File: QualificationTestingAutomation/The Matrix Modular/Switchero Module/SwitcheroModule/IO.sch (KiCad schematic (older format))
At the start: 8 parts, among them J1 Conn_02x32_Counter_Clockwise_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, J2 OBD Connector, J3 OBD Connector, J6 Conn_02x32_Counter_Clockwise_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

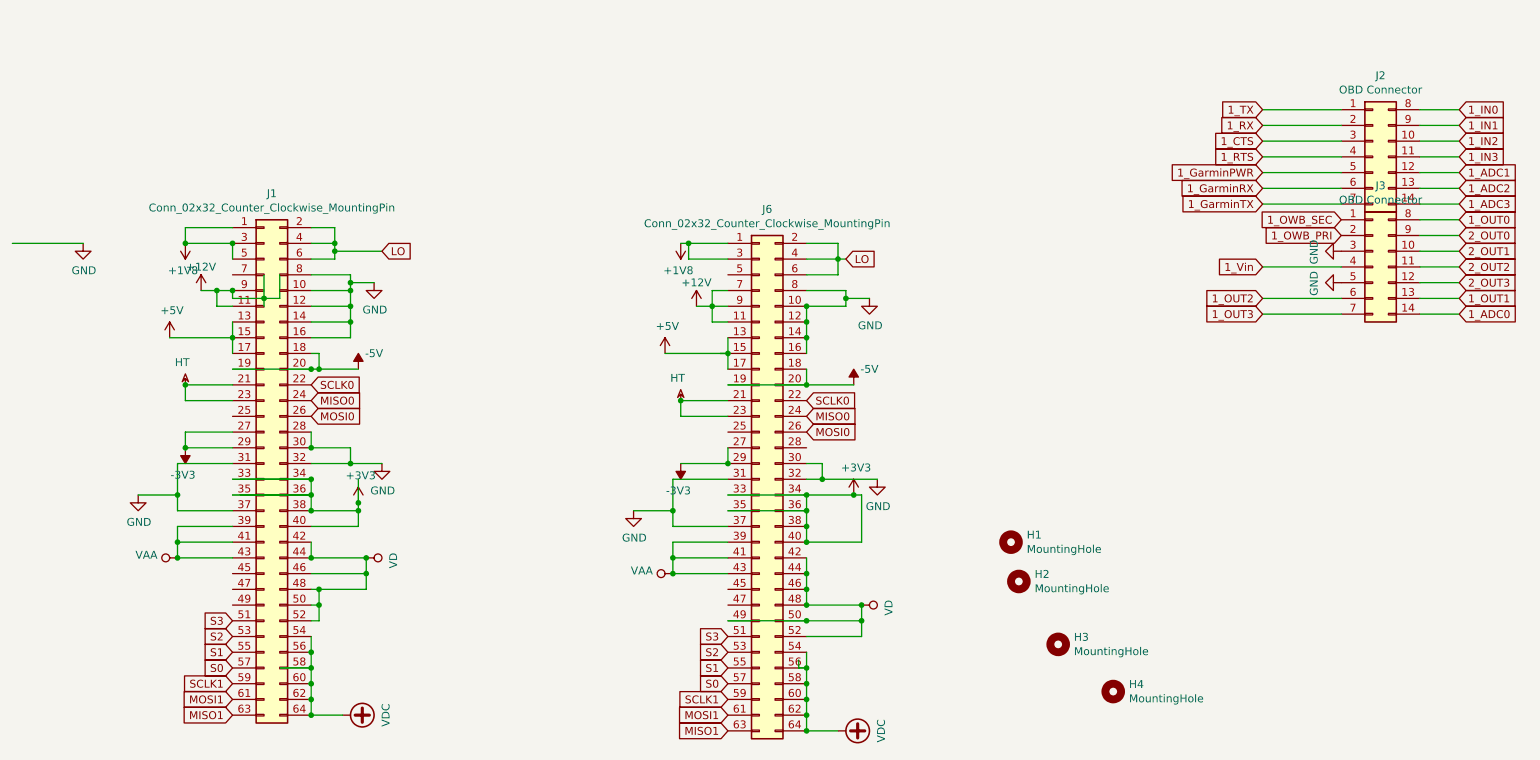
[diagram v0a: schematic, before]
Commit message: Cleaned up the libraries Cleaned up the tracks Adjusted footprints to the manufacturers minimum size.
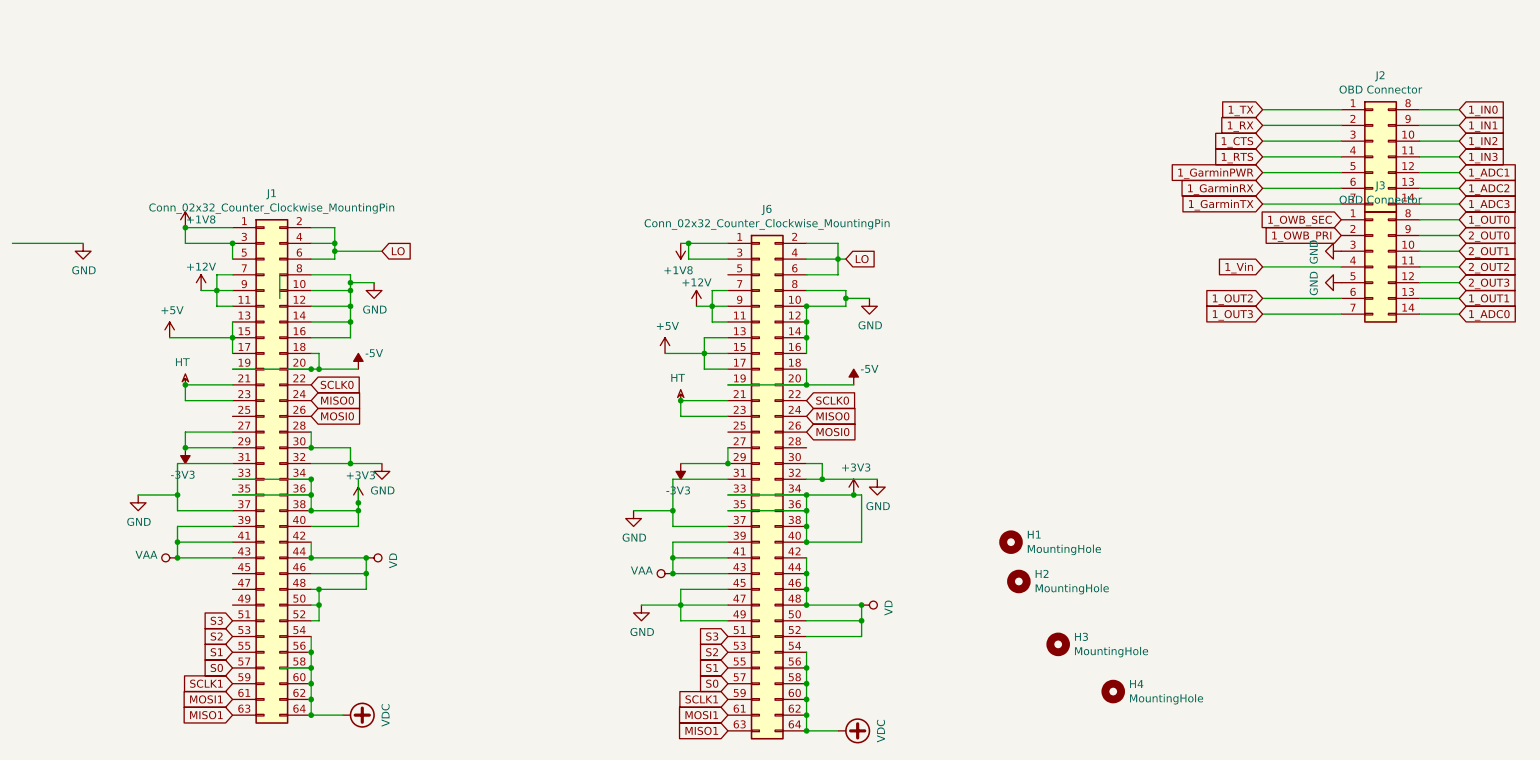
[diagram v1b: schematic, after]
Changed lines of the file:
@@
 L power:+1V8 #PWR?
 U 1 1 5DFE913D
-P 2450 2200
+P 2450 2100
 AR Path="/5D94288A/5DFE913D" Ref="#PWR?"  Part="1"
 AR Path="/5D968A33/5DFE913D" Ref="#PWR?"  Part="1"
 AR Path="/5C90F517/5DFE913D" Ref="#PWR0181"  Part="1"
-F 0 "#PWR0181" H 2450 2050 50  0001 C CNN
-F 1 "+1V8" H 2465 2373 50  0000 C CNN
-F 2 "" H 2450 2200 50  0001 C CNN
-F 3 "" H 2450 2200 50  0001 C CNN
-	1    2450 2200
-	-1   0    0    1
+F 0 "#PWR0181" H 2450 1950 50  0001 C CNN
+F 1 "+1V8" H 2550 2150 50  0000 C CNN
+F 2 "" H 2450 2100 50  0001 C CNN
+F 3 "" H 2450 2100 50  0001 C CNN
+	1    2450 2100
+	1    0    0    -1
 $EndComp
 $Comp
@@
 Wire Wire Line
 	2450 2100 2750 2100
-Connection ~ 2450 2200
 $Comp
 L power:GND #PWR0183
@@
 Wire Wire Line
 	3050 2400 3050 2550
-Wire Wire Line
-	3050 2550 2950 2550
 Wire Wire Line
 	3250 2300 3400 2300
@@
 	1    0    0    -1
 $EndComp
-Wire Wire Line
-	5900 3000 5900 2900
 Text GLabel 5900 5000 0    50   Input ~ 0
 S0
@@
 Text GLabel 6400 3300 2    50   Input ~ 0
 MISO0
-Connection ~ 5900 2900
 Connection ~ 5600 3200
-Wire Wire Line
-	5900 2800 5900 2900
 Text GLabel 5900 4700 0    50   Input ~ 0
 S3
@@
 	3250 5200 3450 5200
 Connection ~ 3250 4900
-Wire Wire Line
-	3250 4800 3250 4700
-Connection ~ 3250 4800
 Connection ~ 3250 3800
 Wire Wire Line
@@
 Wire Wire Line
 	5600 3600 5900 3600
-Wire Wire Line
-	6350 4850 6350 4900
 Wire Wire Line
 	5900 3600 5900 3500
@@
 	5650 2200 5900 2200
 Wire Wire Line
-	3250 4800 3250 4900
-Wire Wire Line
 	6400 3600 6500 3600
 Wire Wire Line
@@
 Wire Wire Line
 	3500 3600 3700 3600
-Wire Wire Line
-	6400 4900 6350 4900
 Wire Wire Line
 	3050 4900 3250 4900
@@
 Wire Wire Line
 	5900 3800 6400 3800
-Wire Wire Line
-	2800 3800 3250 3800
-Wire Wire Line
-	2750 3800 3250 3800
 Wire Wire Line
 	5900 3900 6400 3900
@@
 Wire Wire Line
 	6400 4600 6750 4600
-Wire Wire Line
-	5900 4600 6400 4600
 Connection ~ 6400 4100
 Wire Wire Line
@@
 Connection ~ 6400 3100
 Wire Wire Line
-	5850 2900 5900 2900
-Wire Wire Line
-	5500 2900 5900 2900
-Wire Wire Line
 	3250 3400 3250 3500
 Connection ~ 3550 3850
@@
 	3300 4400 3600 4400
 Wire Wire Line
-	2950 2550 2950 2600
-Wire Wire Line
-	2950 2400 2950 2550
-Connection ~ 2950 2550
-Wire Wire Line
-	2750 2550 2750 2500
-Wire Wire Line
-	2750 2550 2950 2550
-Connection ~ 2750 2500
+	2750 3700 3250 3700
+Wire Wire Line
+	3550 3000 3300 3000
+Wire Wire Line
+	3300 4500 3250 4500
+Wire Wire Line
+	3250 4600 3300 4600
+Wire Wire Line
+	3300 4600 3300 4500
+Connection ~ 3300 4500
+Wire Wire Line
+	3250 4100 3250 4200
+Wire Wire Line
+	3500 2500 3500 2600
+Wire Wire Line
+	3500 2600 3250 2600
+Connection ~ 3500 2500
+Wire Wire Line
+	3250 2700 3500 2700
+Wire Wire Line
+	3500 2700 3500 2600
+Connection ~ 3500 2600
+Wire Wire Line
+	3250 2800 3500 2800
+Wire Wire Line
+	3500 2800 3500 2700
+Connection ~ 3500 2700
+Wire Wire Line
+	3300 2900 3300 3000
+Connection ~ 3300 3000
+Wire Wire Line
+	6400 4200 6400 4300
+Connection ~ 6400 4500
+Connection ~ 6400 4300
+Wire Wire Line
+	6400 4300 6400 4400
+Connection ~ 6400 4400
+Wire Wire Line
+	6400 4400 6400 4500
+Wire Wire Line
+	6400 2600 6400 2700
+Connection ~ 6400 2600
+Connection ~ 6400 2700
+Wire Wire Line
+	6400 2700 6400 2800
+Connection ~ 6400 2800
+Wire Wire Line
+	6400 2800 6400 2900
+Wire Wire Line
+	6400 3100 6400 3000
+Wire Wire Line
+	2750 2800 2350 2800
+Wire Wire Line
+	2750 3800 3250 3800
 Connection ~ 3250 5200
 Wire Wire Line
@@
 Connection ~ 3250 5100
 Wire Wire Line
+	3250 4900 3250 5000
+Wire Wire Line
 	3250 5000 3250 5100
-Wire Wire Line
-	3250 4900 3250 5000
 Connection ~ 3250 5000
+Wire Wire Line
+	3250 4800 3250 4900
+Wire Wire Line
+	3250 4800 3250 4700
+Connection ~ 3250 4800
+Connection ~ 3250 4200
 Connection ~ 3250 3900
-Wire Wire Line
-	2750 3700 3250 3700
-Wire Wire Line
-	2800 3700 3250 3700
 Connection ~ 3250 3700
 Connection ~ 3250 3500
 Connection ~ 2750 2200
 Wire Wire Line
+	3300 3000 3250 3000
+Wire Wire Line
 	2750 3000 3250 3000
-Wire Wire Line
-	3550 3000 3300 3000
 Connection ~ 3250 3000
 $Comp
@@
 	1    0    0    -1
 $EndComp
-Wire Wire Line
-	3300 4500 3250 4500
-Wire Wire Line
-	3250 4600 3300 4600
-Wire Wire Line
-	3300 4600 3300 4500
-Connection ~ 3300 4500
-Wire Wire Line
-	3250 4100 3250 4200
-Connection ~ 3250 4200
-Wire Wire Line
-	3500 2500 3500 2600
-Wire Wire Line
-	3500 2600 3250 2600
-Connection ~ 3500 2500
-Wire Wire Line
-	3250 2700 3500 2700
-Wire Wire Line
-	3500 2700 3500 2600
-Connection ~ 3500 2600
-Wire Wire Line
-	3250 2800 3500 2800
-Wire Wire Line
-	3500 2800 3500 2700
-Connection ~ 3500 2700
-Wire Wire Line
-	3300 2900 3300 3000
-Connection ~ 3300 3000
-Wire Wire Line
-	3300 3000 3250 3000
-Connection ~ 6400 4600
-Wire Wire Line
-	6400 4200 6400 4300
-Connection ~ 6400 4500
-Connection ~ 6400 4300
-Wire Wire Line
-	6400 4300 6400 4400
-Connection ~ 6400 4400
-Wire Wire Line
-	6400 4400 6400 4500
-Wire Wire Line
-	6400 2600 6400 2700
-Connection ~ 6400 2600
-Connection ~ 6400 2700
-Wire Wire Line
-	6400 2700 6400 2800
-Connection ~ 6400 2800
-Wire Wire Line
-	6400 2800 6400 2900
-Wire Wire Line
-	6400 3100 6400 3000
-Wire Wire Line
-	2750 2800 2350 2800
+Connection ~ 2450 2100
+Wire Wire Line
+	2750 2400 2650 2400
+Wire Wire Line
+	2650 2400 2650 2500
+Wire Wire Line
+	5500 2900 5750 2900
+Wire Wire Line
+	5900 2800 5750 2800
+Wire Wire Line
+	5750 2800 5750 2900
+Connection ~ 5750 2900
+Wire Wire Line
+	5750 2900 5900 2900
+Wire Wire Line
+	5900 3000 5750 3000
+Wire Wire Line
+	5750 3000 5750 2900
+Wire Wire Line
+	5900 4600 5600 4600
+Wire Wire Line
+	5600 4600 5600 4500
+Wire Wire Line
+	5600 4400 5900 4400
+Wire Wire Line
+	5900 4500 5600 4500
+Connection ~ 5600 4500
+Wire Wire Line
+	5600 4500 5600 4400
+$Comp
+L power:GND #PWR0118
+U 1 1 5C9FFE52
+P 5350 4500
+F 0 "#PWR0118" H 5350 4250 50  0001 C CNN
+F 1 "GND" H 5355 4327 50  0000 C CNN
+F 2 "" H 5350 4500 50  0001 C CNN
+F 3 "" H 5350 4500 50  0001 C CNN
+	1    5350 4500
+	1    0    0    -1
+$EndComp
+Wire Wire Line
+	5350 4500 5600 4500
 $EndSCHEMATC

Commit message: Added Voltage and current measurment of the muxes and relays to the MSP Some clean up of the tracks.
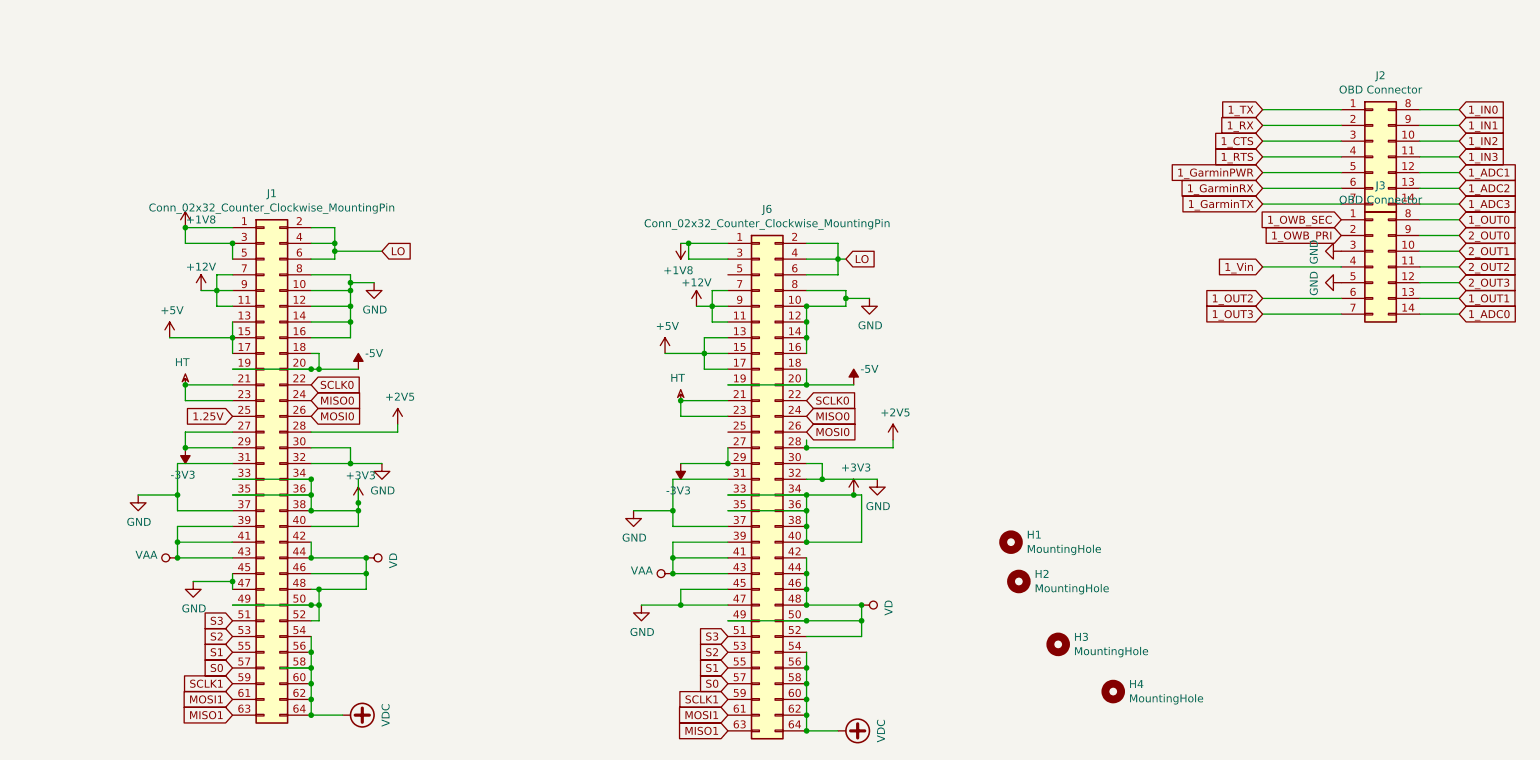
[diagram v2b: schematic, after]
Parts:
- J1, J6: footprint Connector_PinHeader_2.00mm:PinHeader_2x32_P2.00mm_Horizontal -> Connector:PinHeader_2x32_P2.00mm_VerticalOpp
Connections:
- net labels added: +2V5, 1.25V
- wire segments 191 -> 196
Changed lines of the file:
@@
 EESchema Schematic File Version 4
 LIBS:SwitcheroModule-cache
-EELAYER 26 0
+EELAYER 29 0
 EELAYER END
 $Descr A4 11693 8268
@@
 	1    0    0    -1
 $EndComp
-$Comp
-L power:GND #PWR0182
-U 1 1 5DFE914C
-P 1800 2200
-F 0 "#PWR0182" H 1800 1950 50  0001 C CNN
-F 1 "GND" H 1805 2027 50  0000 C CNN
-F 2 "" H 1800 2200 50  0001 C CNN
-F 3 "" H 1800 2200 50  0001 C CNN
-	1    1800 2200
-	1    0    0    -1
-$EndComp
-Wire Wire Line
-	1800 2200 1350 2200
 Wire Wire Line
 	3500 2400 3500 2450
@@
 Wire Wire Line
 	2750 3900 2400 3900
-Wire Wire Line
-	3050 2400 3050 2550
 Wire Wire Line
 	3250 2300 3400 2300
@@
 F 0 "J6" H 6150 5417 50  0000 C CNN
 F 1 "Conn_02x32_Counter_Clockwise_MountingPin" H 6150 5326 50  0000 C CNN
-F 2 "Connector_PinHeader_2.00mm:PinHeader_2x32_P2.00mm_Horizontal" H 6100 3700 50  0001 C CNN
+F 2 "Connector:PinHeader_2x32_P2.00mm_VerticalOpp" H 6100 3700 50  0001 C CNN
 F 3 "~" H 6100 3700 50  0001 C CNN
 	1    6100 3700
@@
 $EndComp
 Connection ~ 6400 3100
-Wire Wire Line
-	3250 3400 3250 3500
 Connection ~ 3550 3850
 Wire Wire Line
@@
 Connection ~ 3250 3900
 Connection ~ 3250 3700
-Connection ~ 3250 3500
 Connection ~ 2750 2200
 Wire Wire Line
@@
 F 0 "J1" H 3000 5317 50  0000 C CNN
 F 1 "Conn_02x32_Counter_Clockwise_MountingPin" H 3000 5226 50  0000 C CNN
-F 2 "Connector_PinHeader_2.00mm:PinHeader_2x32_P2.00mm_Horizontal" H 2950 3600 50  0001 C CNN
+F 2 "Connector:PinHeader_2x32_P2.00mm_VerticalOpp" H 2950 3600 50  0001 C CNN
 F 3 "~" H 2950 3600 50  0001 C CNN
 	1    2950 3600
@@
 Wire Wire Line
 	5750 3000 5750 2900
-Wire Wire Line
-	5900 4600 5600 4600
-Wire Wire Line
-	5600 4600 5600 4500
 Wire Wire Line
 	5600 4400 5900 4400
@@
 Wire Wire Line
 	5350 4500 5600 4500
+Connection ~ 3250 4500
+Wire Wire Line
+	3250 4500 2750 4500
+Wire Wire Line
+	5900 4600 6400 4600
+Connection ~ 6400 4600
+Wire Wire Line
+	2750 4400 2750 4350
+$Comp
+L power:GND #PWR?
+U 1 1 5C9ED4D8
+P 2500 4350
+F 0 "#PWR?" H 2500 4100 50  0001 C CNN
+F 1 "GND" H 2505 4177 50  0000 C CNN
+F 2 "" H 2500 4350 50  0001 C CNN
+F 3 "" H 2500 4350 50  0001 C CNN
+	1    2500 4350
+	1    0    0    -1
+$EndComp
+Wire Wire Line
+	2500 4350 2750 4350
+Connection ~ 2750 4350
+Wire Wire Line
+	2750 4350 2750 4300
+$Comp
+L power:+2V5 #PWR?
+U 1 1 5CA019EC
+P 6950 3450
+F 0 "#PWR?" H 6950 3300 50  0001 C CNN
+F 1 "+2V5" H 6965 3623 50  0000 C CNN
+F 2 "" H 6950 3450 50  0001 C CNN
+F 3 "" H 6950 3450 50  0001 C CNN
+	1    6950 3450
+	1    0    0    -1
+$EndComp
+Wire Wire Line
+	6950 3500 6400 3500
+Wire Wire Line
+	6400 3450 6400 3500
+Connection ~ 6400 3500
+Wire Wire Line
+	6950 3500 6950 3450
+$Comp
+L power:+2V5 #PWR?
+U 1 1 5CA2505E
+P 3800 3350
+F 0 "#PWR?" H 3800 3200 50  0001 C CNN
+F 1 "+2V5" H 3815 3523 50  0000 C CNN
+F 2 "" H 3800 3350 50  0001 C CNN
+F 3 "" H 3800 3350 50  0001 C CNN
+	1    3800 3350
+	1    0    0    -1
+$EndComp
+Wire Wire Line
+	3800 3400 3250 3400
+Wire Wire Line
+	3800 3400 3800 3350
+Text GLabel 2750 3300 0    50   Input ~ 0
+1.25V
 $EndSCHEMATC

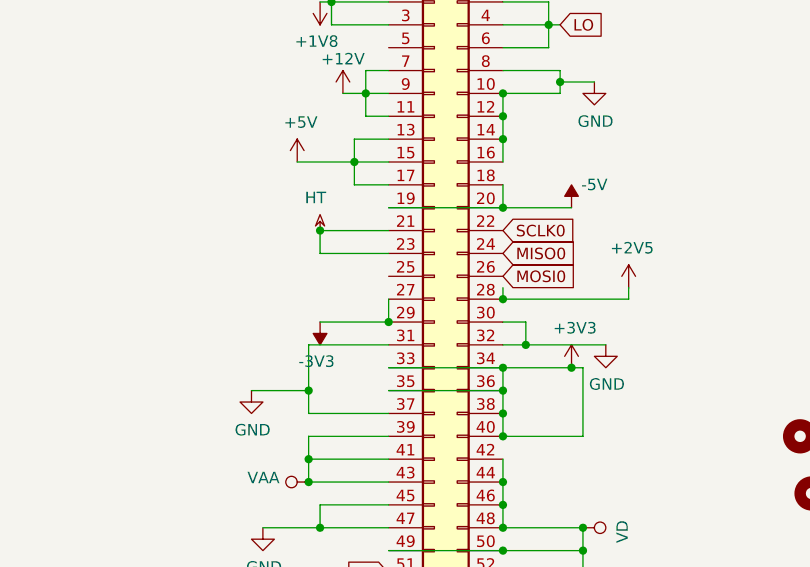
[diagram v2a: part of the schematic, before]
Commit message: Updated the layout to accomodate the voltage and current sensing.
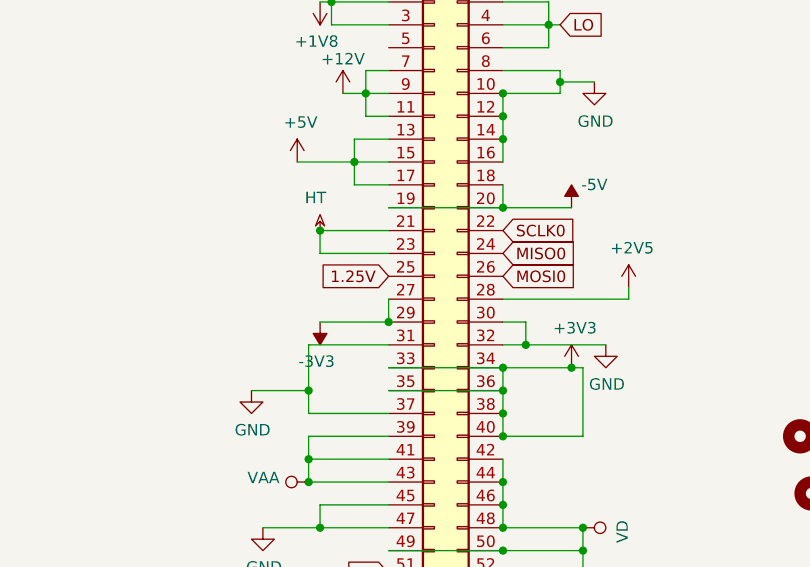
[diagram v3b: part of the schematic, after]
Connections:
- net 1.25V: now also J6.25 (Pin_25)
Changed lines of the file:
@@
 	6950 3500 6400 3500
-Wire Wire Line
-	6400 3450 6400 3500
-Connection ~ 6400 3500
 Wire Wire Line
 	6950 3500 6950 3450
@@
 Text GLabel 2750 3300 0    50   Input ~ 0
 1.25V
+Text GLabel 5900 3400 0    50   Input ~ 0
+1.25V
 $EndSCHEMATC
